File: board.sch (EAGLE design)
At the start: 17 parts

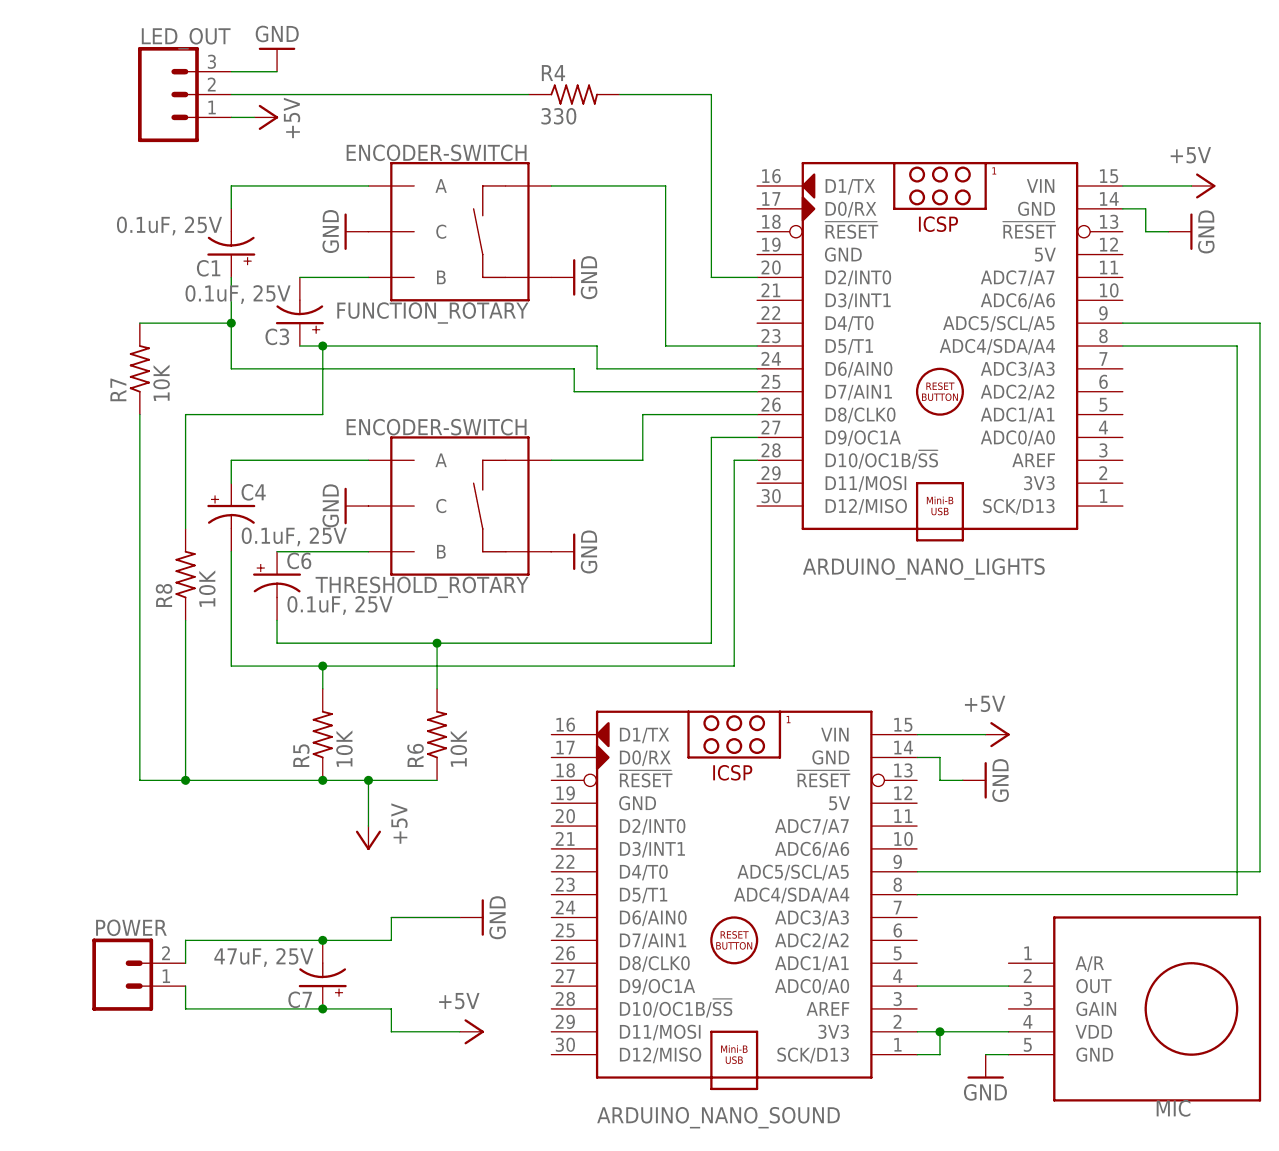
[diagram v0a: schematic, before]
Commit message: fixing mistakes from prototype
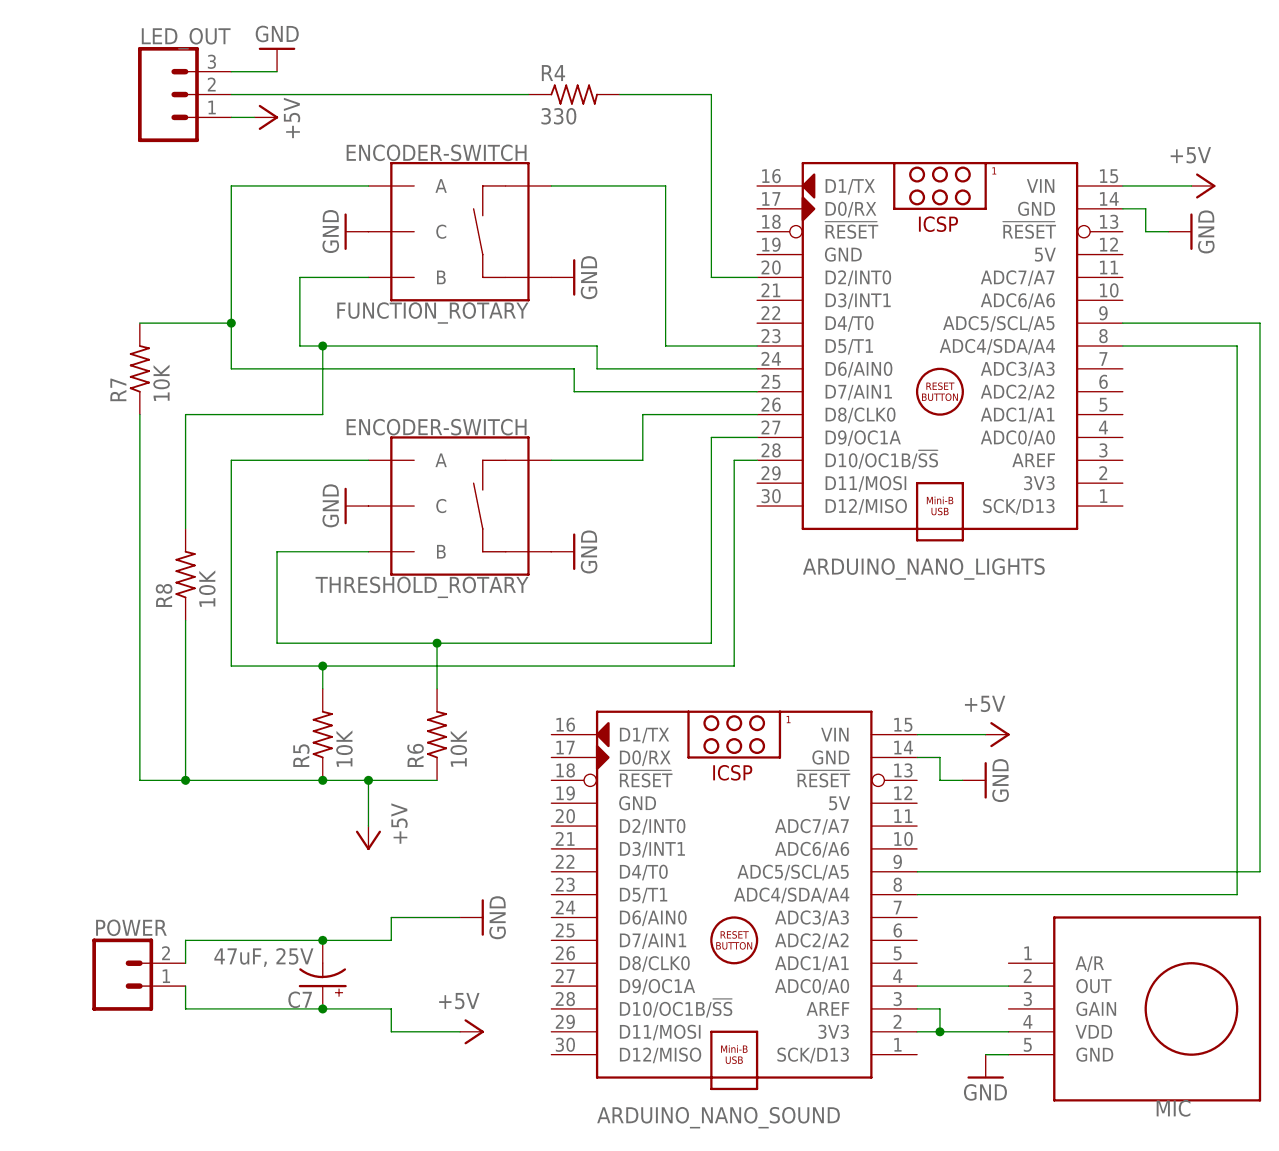
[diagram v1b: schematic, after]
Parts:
- removed C1, C3, C4, C6: 0.1uF, 25V, rcl:CPOL-USE2-4
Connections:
- removed net N$16: C6.+, THRESHOLD_ROTARY.B
- removed net N$4: ARDUINO_NANO_LIGHTS.D7/AIN1, C1.+, R7.2
- removed net N$6: ARDUINO_NANO_LIGHTS.D6/AIN0, C3.+, R8.2
- removed net N$7: ARDUINO_NANO_LIGHTS.D10/OC1B/!SS, C4.-, R5.2
- net MIC_VCC: now also ARDUINO_NANO_SOUND.AREF; no longer ARDUINO_NANO_SOUND.SCK/D13
- net N$13: now also ARDUINO_NANO_LIGHTS.D7/AIN1, R7.2; no longer C1.-
- net N$14: now also ARDUINO_NANO_LIGHTS.D6/AIN0, R8.2; no longer C3.-
- net N$15: now also ARDUINO_NANO_LIGHTS.D10/OC1B/!SS, R5.2; no longer C4.+
- net N$2: now also THRESHOLD_ROTARY.B; no longer C6.-
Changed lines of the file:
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@@
 <part name="GND4" library="supply1" deviceset="GND" device=""/>
 <part name="GND7" library="supply1" deviceset="GND" device=""/>
-<part name="C1" library="rcl" library_urn="urn:adsk.eagle:library:334" deviceset="CPOL-US" device="E2-4" package3d_urn="urn:adsk.eagle:package:23347/1" value="0.1uF, 25V"/>
-<part name="C3" library="rcl" library_urn="urn:adsk.eagle:library:334" deviceset="CPOL-US" device="E2-4" package3d_urn="urn:adsk.eagle:package:23347/1" value="0.1uF, 25V"/>
-<part name="C4" library="rcl" library_urn="urn:adsk.eagle:library:334" deviceset="CPOL-US" device="E2-4" package3d_urn="urn:adsk.eagle:package:23347/1" value="0.1uF, 25V"/>
-<part name="C6" library="rcl" library_urn="urn:adsk.eagle:library:334" deviceset="CPOL-US" device="E2-4" package3d_urn="urn:adsk.eagle:package:23347/1" value="0.1uF, 25V"/>
 <part name="C7" library="rcl" library_urn="urn:adsk.eagle:library:334" deviceset="CPOL-US" device="E2-5" package3d_urn="urn:adsk.eagle:package:23346/2" value="47uF, 25V"/>
 <part name="R4" library="adafruit" library_urn="urn:adsk.eagle:library:420" deviceset="R-US_" device="0207/7" package3d_urn="urn:adsk.eagle:package:6240602/1" value="330"/>
@@
 <attribute name="VALUE" x="-12.7" y="134.62" size="1.778" layer="96" rot="R270"/>
 </instance>
-<instance part="C1" gate="G$1" x="-22.86" y="129.54" smashed="yes" rot="R180">
-<attribute name="NAME" x="-23.876" y="128.905" size="1.778" layer="95" rot="R180"/>
-<attribute name="VALUE" x="-23.876" y="133.731" size="1.778" layer="96" rot="R180"/>
-</instance>
-<instance part="C3" gate="G$1" x="-15.24" y="121.92" smashed="yes" rot="R180">
-<attribute name="NAME" x="-16.256" y="121.285" size="1.778" layer="95" rot="R180"/>
-<attribute name="VALUE" x="-16.256" y="126.111" size="1.778" layer="96" rot="R180"/>
-</instance>
-<instance part="C4" gate="G$1" x="-22.86" y="101.6" smashed="yes">
-<attribute name="NAME" x="-21.844" y="102.235" size="1.778" layer="95"/>
-<attribute name="VALUE" x="-21.844" y="97.409" size="1.778" layer="96"/>
-</instance>
-<instance part="C6" gate="G$1" x="-17.78" y="93.98" smashed="yes">
-<attribute name="NAME" x="-16.764" y="94.615" size="1.778" layer="95"/>
-<attribute name="VALUE" x="-16.764" y="89.789" size="1.778" layer="96"/>
-</instance>
 <instance part="C7" gate="G$1" x="-12.7" y="48.26" smashed="yes" rot="R180">
 <attribute name="NAME" x="-13.716" y="47.625" size="1.778" layer="95" rot="R180"/>
@@
 <wire x1="30.48" y1="86.36" x2="30.48" y2="109.22" width="0.1524" layer="91"/>
 <wire x1="30.48" y1="109.22" x2="35.56" y2="109.22" width="0.1524" layer="91"/>
-<pinref part="C6" gate="G$1" pin="-"/>
-<wire x1="-17.78" y1="86.36" x2="-17.78" y2="88.9" width="0.1524" layer="91"/>
 <pinref part="R6" gate="G$1" pin="2"/>
 <wire x1="0" y1="81.28" x2="0" y2="86.36" width="0.1524" layer="91"/>
 <junction x="0" y="86.36"/>
+<pinref part="THRESHOLD_ROTARY" gate="G$1" pin="B"/>
+<wire x1="-17.78" y1="96.52" x2="-7.62" y2="96.52" width="0.1524" layer="91"/>
+<wire x1="-17.78" y1="86.36" x2="-17.78" y2="96.52" width="0.1524" layer="91"/>
 </segment>
 </net>
@@
 </segment>
 </net>
-<net name="N$4" class="0">
-<segment>
+<net name="N$13" class="0">
+<segment>
+<pinref part="FUNCTION_ROTARY" gate="G$1" pin="A"/>
+<wire x1="-7.62" y1="137.16" x2="-22.86" y2="137.16" width="0.1524" layer="91"/>
 <wire x1="-22.86" y1="116.84" x2="15.24" y2="116.84" width="0.1524" layer="91"/>
 <pinref part="ARDUINO_NANO_LIGHTS" gate="G$1" pin="D7/AIN1"/>
 <wire x1="15.24" y1="116.84" x2="15.24" y2="114.3" width="0.1524" layer="91"/>
 <wire x1="15.24" y1="114.3" x2="35.56" y2="114.3" width="0.1524" layer="91"/>
-<pinref part="C1" gate="G$1" pin="+"/>
-<wire x1="-22.86" y1="127" x2="-22.86" y2="121.92" width="0.1524" layer="91"/>
 <pinref part="R7" gate="G$1" pin="2"/>
 <wire x1="-22.86" y1="121.92" x2="-22.86" y2="116.84" width="0.1524" layer="91"/>
 <wire x1="-33.02" y1="121.92" x2="-22.86" y2="121.92" width="0.1524" layer="91"/>
 <junction x="-22.86" y="121.92"/>
-</segment>
-</net>
-<net name="N$6" class="0">
-<segment>
+<wire x1="-22.86" y1="137.16" x2="-22.86" y2="121.92" width="0.1524" layer="91"/>
+</segment>
+</net>
+<net name="N$14" class="0">
+<segment>
+<pinref part="FUNCTION_ROTARY" gate="G$1" pin="B"/>
+<wire x1="-15.24" y1="127" x2="-7.62" y2="127" width="0.1524" layer="91"/>
 <wire x1="-15.24" y1="119.38" x2="-12.7" y2="119.38" width="0.1524" layer="91"/>
 <pinref part="ARDUINO_NANO_LIGHTS" gate="G$1" pin="D6/AIN0"/>
@@
 <wire x1="17.78" y1="119.38" x2="17.78" y2="116.84" width="0.1524" layer="91"/>
 <wire x1="17.78" y1="116.84" x2="35.56" y2="116.84" width="0.1524" layer="91"/>
-<pinref part="C3" gate="G$1" pin="+"/>
 <pinref part="R8" gate="G$1" pin="2"/>
 <wire x1="-27.94" y1="99.06" x2="-27.94" y2="111.76" width="0.1524" layer="91"/>
@@
 <wire x1="-12.7" y1="111.76" x2="-12.7" y2="119.38" width="0.1524" layer="91"/>
 <junction x="-12.7" y="119.38"/>
-</segment>
-</net>
-<net name="N$13" class="0">
-<segment>
-<pinref part="FUNCTION_ROTARY" gate="G$1" pin="A"/>
-<wire x1="-7.62" y1="137.16" x2="-22.86" y2="137.16" width="0.1524" layer="91"/>
-<pinref part="C1" gate="G$1" pin="-"/>
-<wire x1="-22.86" y1="137.16" x2="-22.86" y2="134.62" width="0.1524" layer="91"/>
-</segment>
-</net>
-<net name="N$14" class="0">
-<segment>
-<pinref part="C3" gate="G$1" pin="-"/>
-<pinref part="FUNCTION_ROTARY" gate="G$1" pin="B"/>
-<wire x1="-15.24" y1="127" x2="-7.62" y2="127" width="0.1524" layer="91"/>
+<wire x1="-15.24" y1="127" x2="-15.24" y2="119.38" width="0.1524" layer="91"/>
 </segment>
 </net>
@@
 <segment>
 <pinref part="THRESHOLD_ROTARY" gate="G$1" pin="A"/>
-<pinref part="C4" gate="G$1" pin="+"/>
 <wire x1="-7.62" y1="106.68" x2="-22.86" y2="106.68" width="0.1524" layer="91"/>
-<wire x1="-22.86" y1="106.68" x2="-22.86" y2="104.14" width="0.1524" layer="91"/>
-</segment>
-</net>
-<net name="N$16" class="0">
-<segment>
-<pinref part="C6" gate="G$1" pin="+"/>
-<pinref part="THRESHOLD_ROTARY" gate="G$1" pin="B"/>
-<wire x1="-17.78" y1="96.52" x2="-7.62" y2="96.52" width="0.1524" layer="91"/>
+<pinref part="ARDUINO_NANO_LIGHTS" gate="G$1" pin="D10/OC1B/!SS"/>
+<wire x1="35.56" y1="106.68" x2="33.02" y2="106.68" width="0.1524" layer="91"/>
+<wire x1="33.02" y1="106.68" x2="33.02" y2="83.82" width="0.1524" layer="91"/>
+<pinref part="R5" gate="G$1" pin="2"/>
+<wire x1="33.02" y1="83.82" x2="-12.7" y2="83.82" width="0.1524" layer="91"/>
+<wire x1="-12.7" y1="83.82" x2="-12.7" y2="81.28" width="0.1524" layer="91"/>
+<wire x1="-12.7" y1="83.82" x2="-22.86" y2="83.82" width="0.1524" layer="91"/>
+<wire x1="-22.86" y1="83.82" x2="-22.86" y2="106.68" width="0.1524" layer="91"/>
+<junction x="-12.7" y="83.82"/>
 </segment>
 </net>
@@
 <net name="MIC_VCC" class="0">
 <segment>
-<pinref part="ARDUINO_NANO_SOUND" gate="G$1" pin="SCK/D13"/>
-<wire x1="53.34" y1="40.64" x2="55.88" y2="40.64" width="0.1524" layer="91"/>
-<wire x1="55.88" y1="40.64" x2="55.88" y2="43.18" width="0.1524" layer="91"/>
 <pinref part="MIC" gate="G$1" pin="VDD"/>
 <wire x1="63.5" y1="43.18" x2="55.88" y2="43.18" width="0.1524" layer="91"/>
 <pinref part="ARDUINO_NANO_SOUND" gate="G$1" pin="3V3"/>
-<wire x1="53.34" y1="43.18" x2="55.88" y2="43.18" width="0.1524" layer="91"/>
+<pinref part="ARDUINO_NANO_SOUND" gate="G$1" pin="AREF"/>
+<wire x1="55.88" y1="43.18" x2="53.34" y2="43.18" width="0.1524" layer="91"/>
+<wire x1="55.88" y1="43.18" x2="55.88" y2="45.72" width="0.1524" layer="91"/>
+<wire x1="55.88" y1="45.72" x2="53.34" y2="45.72" width="0.1524" layer="91"/>
 <junction x="55.88" y="43.18"/>
 </segment>
@@
 </segment>
 </net>
-<net name="N$7" class="0">
-<segment>
-<pinref part="ARDUINO_NANO_LIGHTS" gate="G$1" pin="D10/OC1B/!SS"/>
-<wire x1="35.56" y1="106.68" x2="33.02" y2="106.68" width="0.1524" layer="91"/>
-<wire x1="33.02" y1="106.68" x2="33.02" y2="83.82" width="0.1524" layer="91"/>
-<pinref part="R5" gate="G$1" pin="2"/>
-<wire x1="33.02" y1="83.82" x2="-12.7" y2="83.82" width="0.1524" layer="91"/>
-<wire x1="-12.7" y1="83.82" x2="-12.7" y2="81.28" width="0.1524" layer="91"/>
-<pinref part="C4" gate="G$1" pin="-"/>
-<wire x1="-12.7" y1="83.82" x2="-22.86" y2="83.82" width="0.1524" layer="91"/>
-<wire x1="-22.86" y1="83.82" x2="-22.86" y2="96.52" width="0.1524" layer="91"/>
-<junction x="-12.7" y="83.82"/>
-</segment>
-</net>

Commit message: Updating schematic
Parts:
- removed C7: 47uF, 25V, rcl:CPOL-USE2-5
- removed POWER: (no value), SparkFun-Connectors:CONN_02
- removed R5, R6, R8: 10K, adafruit:R-US_0207/7
- added C1: 47uF 25V, adafruit:CPOL-USE2-5
- added R1, R2, R3: 10K, adafruit:R-US_0207/7
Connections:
- removed net N$14: ARDUINO_NANO_LIGHTS.D6/AIN0, FUNCTION_ROTARY.B, R8.2
- new net N$4: ARDUINO_NANO_LIGHTS.D6/AIN0, FUNCTION_ROTARY.B, R1.2
- net +5V: now also C1.+, R1.1, R2.1, R3.1; no longer C7.+, POWER.1, R5.1, R6.1, R8.1
- net GND: now also C1.-; no longer C7.-, POWER.2
- net N$15: now also R2.2; no longer R5.2
- net N$2: now also R3.2; no longer R6.2
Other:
- moved on the sheet: ARDUINO_NANO_SOUND, R7

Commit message: V2, applying learnings from V1
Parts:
- removed R1, R2, R3, R7: 10K, adafruit:R-US_0207/7
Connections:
- net +5V: no longer R1.1, R2.1, R3.1, R7.1
- net N$13: no longer R7.2
- net N$15: no longer R2.2
- net N$2: no longer R3.2
- net N$4: no longer R1.2
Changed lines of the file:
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@@
 <part name="GND14" library="supply1" deviceset="GND" device=""/>
 <part name="GND15" library="supply1" deviceset="GND" device=""/>
-<part name="R7" library="adafruit" library_urn="urn:adsk.eagle:library:420" deviceset="R-US_" device="0207/7" package3d_urn="urn:adsk.eagle:package:6240602/1" value="10K"/>
 <part name="P+4" library="supply1" library_urn="urn:adsk.eagle:library:371" deviceset="+5V" device=""/>
 <part name="P+5" library="supply1" library_urn="urn:adsk.eagle:library:371" deviceset="+5V" device=""/>
@@
 <part name="MIC" library="toepferg" deviceset="ADAFRUIT_ELECTRET_MIC_MAX9817" device=""/>
 <part name="GND16" library="supply1" deviceset="GND" device=""/>
-<part name="P+1" library="supply1" library_urn="urn:adsk.eagle:library:371" deviceset="+5V" device=""/>
-<part name="R1" library="adafruit" library_urn="urn:adsk.eagle:library:420" deviceset="R-US_" device="0207/7" package3d_urn="urn:adsk.eagle:package:6240602/1" value="10K"/>
-<part name="P+7" library="supply1" library_urn="urn:adsk.eagle:library:371" deviceset="+5V" device=""/>
-<part name="R2" library="adafruit" library_urn="urn:adsk.eagle:library:420" deviceset="R-US_" device="0207/7" package3d_urn="urn:adsk.eagle:package:6240602/1" value="10K"/>
-<part name="P+8" library="supply1" library_urn="urn:adsk.eagle:library:371" deviceset="+5V" device=""/>
-<part name="R3" library="adafruit" library_urn="urn:adsk.eagle:library:420" deviceset="R-US_" device="0207/7" package3d_urn="urn:adsk.eagle:package:6240602/1" value="10K"/>
-<part name="P+9" library="supply1" library_urn="urn:adsk.eagle:library:371" deviceset="+5V" device=""/>
 <part name="P+2" library="supply1" library_urn="urn:adsk.eagle:library:371" deviceset="+5V" device=""/>
 <part name="GND2" library="supply1" deviceset="GND" device=""/>
@@
 <attribute name="VALUE" x="-15.24" y="154.94" size="1.778" layer="96" rot="R180"/>
 </instance>
-<instance part="R7" gate="G$1" x="-30.48" y="137.16" smashed="yes">
-<attribute name="NAME" x="-34.29" y="138.6586" size="1.778" layer="95"/>
-<attribute name="VALUE" x="-34.29" y="133.858" size="1.778" layer="96"/>
-</instance>
 <instance part="P+4" gate="1" x="-17.78" y="144.78" smashed="yes" rot="R270">
 <attribute name="VALUE" x="-15.24" y="142.24" size="1.778" layer="96" rot="R90"/>
@@
 <instance part="GND16" gate="1" x="60.96" y="38.1" smashed="yes">
 <attribute name="VALUE" x="58.42" y="35.56" size="1.778" layer="96"/>
-</instance>
-<instance part="P+1" gate="1" x="-43.18" y="137.16" smashed="yes" rot="R90">
-<attribute name="VALUE" x="-38.1" y="134.62" size="1.778" layer="96" rot="R180"/>
-</instance>
-<instance part="R1" gate="G$1" x="-25.4" y="127" smashed="yes">
-<attribute name="NAME" x="-29.21" y="128.4986" size="1.778" layer="95"/>
-<attribute name="VALUE" x="-29.21" y="123.698" size="1.778" layer="96"/>
-</instance>
-<instance part="P+7" gate="1" x="-38.1" y="127" smashed="yes" rot="R90">
-<attribute name="VALUE" x="-33.02" y="124.46" size="1.778" layer="96" rot="R180"/>
-</instance>
-<instance part="R2" gate="G$1" x="-33.02" y="106.68" smashed="yes">
-<attribute name="NAME" x="-36.83" y="108.1786" size="1.778" layer="95"/>
-<attribute name="VALUE" x="-36.83" y="103.378" size="1.778" layer="96"/>
-</instance>
-<instance part="P+8" gate="1" x="-45.72" y="106.68" smashed="yes" rot="R90">
-<attribute name="VALUE" x="-40.64" y="104.14" size="1.778" layer="96" rot="R180"/>
-</instance>
-<instance part="R3" gate="G$1" x="-27.94" y="96.52" smashed="yes">
-<attribute name="NAME" x="-31.75" y="98.0186" size="1.778" layer="95"/>
-<attribute name="VALUE" x="-31.75" y="93.218" size="1.778" layer="96"/>
-</instance>
-<instance part="P+9" gate="1" x="-40.64" y="96.52" smashed="yes" rot="R90">
-<attribute name="VALUE" x="-35.56" y="93.98" size="1.778" layer="96" rot="R180"/>
 </instance>
 <instance part="P+2" gate="1" x="-27.94" y="76.2" smashed="yes">
@@
 <wire x1="-17.78" y1="96.52" x2="-7.62" y2="96.52" width="0.1524" layer="91"/>
 <wire x1="-17.78" y1="86.36" x2="-17.78" y2="96.52" width="0.1524" layer="91"/>
-<pinref part="R3" gate="G$1" pin="2"/>
-<wire x1="-17.78" y1="96.52" x2="-22.86" y2="96.52" width="0.1524" layer="91"/>
-<junction x="-17.78" y="96.52"/>
 </segment>
 </net>
@@
 <wire x1="12.7" y1="114.3" x2="35.56" y2="114.3" width="0.1524" layer="91"/>
 <wire x1="-17.78" y1="137.16" x2="-17.78" y2="116.84" width="0.1524" layer="91"/>
-<pinref part="R7" gate="G$1" pin="2"/>
-<wire x1="-17.78" y1="137.16" x2="-25.4" y2="137.16" width="0.1524" layer="91"/>
-<junction x="-17.78" y="137.16"/>
 </segment>
 </net>
@@
 <wire x1="33.02" y1="83.82" x2="-20.32" y2="83.82" width="0.1524" layer="91"/>
 <wire x1="-20.32" y1="83.82" x2="-20.32" y2="106.68" width="0.1524" layer="91"/>
-<pinref part="R2" gate="G$1" pin="2"/>
-<wire x1="-20.32" y1="106.68" x2="-27.94" y2="106.68" width="0.1524" layer="91"/>
-<junction x="-20.32" y="106.68"/>
 </segment>
 </net>
@@
 <pinref part="P+4" gate="1" pin="+5V"/>
 <wire x1="-22.86" y1="144.78" x2="-20.32" y2="144.78" width="0.1524" layer="91"/>
-</segment>
-<segment>
-<pinref part="R7" gate="G$1" pin="1"/>
-<pinref part="P+1" gate="1" pin="+5V"/>
-<wire x1="-35.56" y1="137.16" x2="-40.64" y2="137.16" width="0.1524" layer="91"/>
-</segment>
-<segment>
-<pinref part="R1" gate="G$1" pin="1"/>
-<pinref part="P+7" gate="1" pin="+5V"/>
-<wire x1="-30.48" y1="127" x2="-35.56" y2="127" width="0.1524" layer="91"/>
-</segment>
-<segment>
-<pinref part="R2" gate="G$1" pin="1"/>
-<pinref part="P+8" gate="1" pin="+5V"/>
-<wire x1="-38.1" y1="106.68" x2="-43.18" y2="106.68" width="0.1524" layer="91"/>
-</segment>
-<segment>
-<pinref part="R3" gate="G$1" pin="1"/>
-<pinref part="P+9" gate="1" pin="+5V"/>
-<wire x1="-33.02" y1="96.52" x2="-38.1" y2="96.52" width="0.1524" layer="91"/>
 </segment>
 <segment>
@@
 <net name="N$4" class="0">
 <segment>
-<pinref part="R1" gate="G$1" pin="2"/>
-<wire x1="-15.24" y1="127" x2="-20.32" y2="127" width="0.1524" layer="91"/>
 <pinref part="FUNCTION_ROTARY" gate="G$1" pin="B"/>
 <wire x1="-15.24" y1="127" x2="-7.62" y2="127" width="0.1524" layer="91"/>
@@
 <wire x1="17.78" y1="116.84" x2="35.56" y2="116.84" width="0.1524" layer="91"/>
 <wire x1="-15.24" y1="127" x2="-15.24" y2="119.38" width="0.1524" layer="91"/>
-<junction x="-15.24" y="127"/>
 </segment>
 </net>
@@
 </sheet>
 </sheets>
+<errors>
+</errors>
 </schematic>
 </drawing>
